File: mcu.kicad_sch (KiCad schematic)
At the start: 18 parts

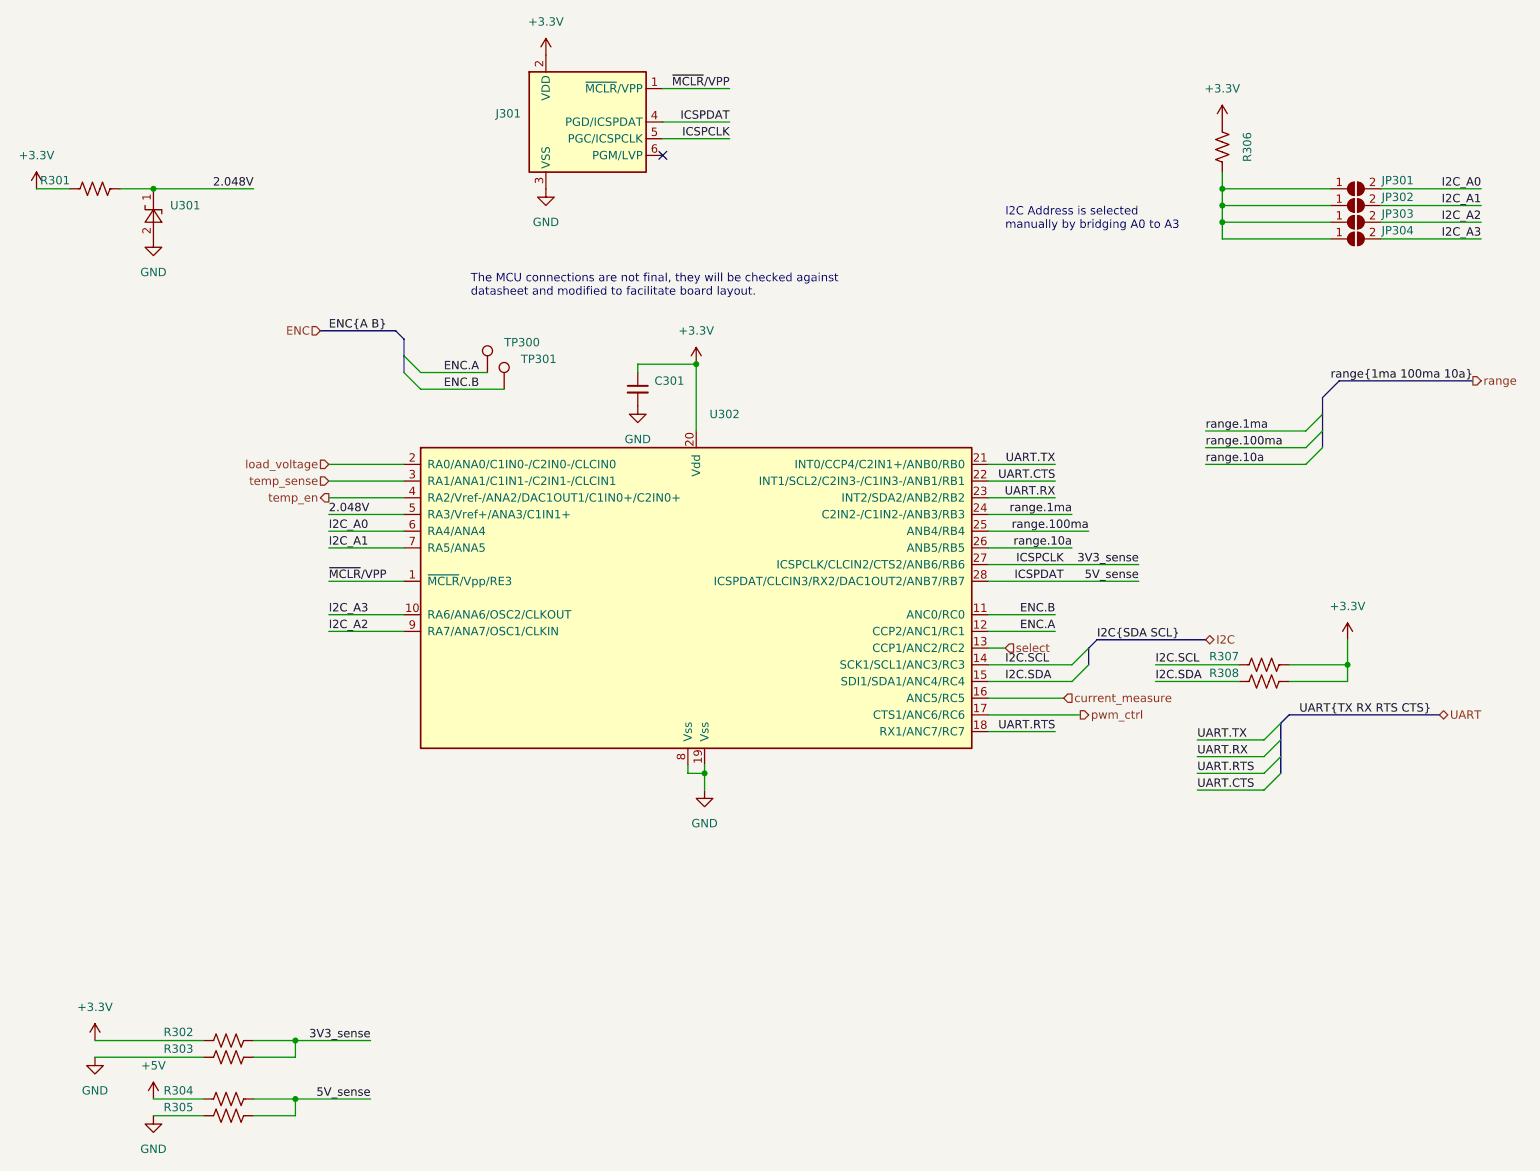
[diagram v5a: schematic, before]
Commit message: Reduce trace resistance of 10mOhm channel
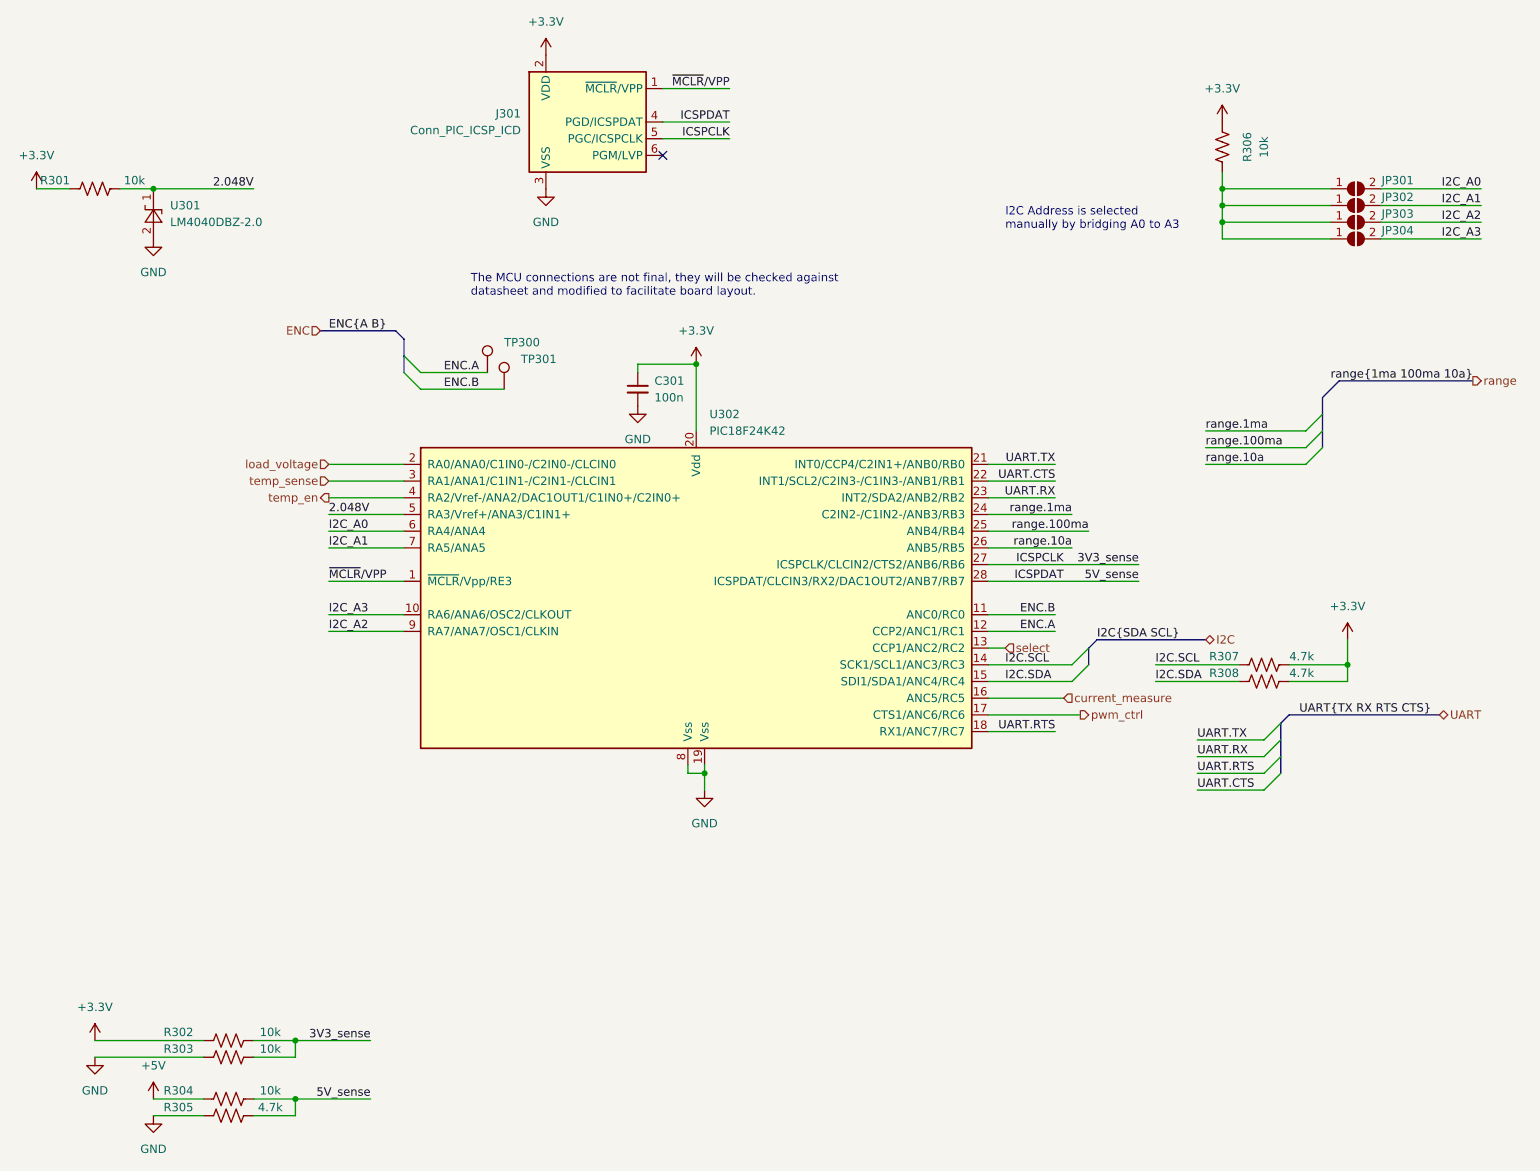
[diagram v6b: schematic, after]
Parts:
- C301: value (none) -> 100n; footprint (none) -> Capacitor_SMD:C_0402_1005Metric
- J301: value (none) -> Conn_PIC_ICSP_ICD; footprint (none) -> Connector_PinHeader_2.54mm:PinHeader_1x06_P2.54mm_Vertical
- JP301, JP302, JP303, JP304: value (none) -> SB; footprint (none) -> Jumper:SolderJumper-2_P1.3mm_Open_TrianglePad1.0x1.5mm
- R301, R302, R303, R304, R306: value (none) -> 10k; footprint (none) -> Resistor_SMD:R_0805_2012Metric
- R305, R307, R308: value (none) -> 4.7k; footprint (none) -> Resistor_SMD:R_0805_2012Metric
- TP300, TP301: value (none) -> ~; footprint (none) -> TestPoint:TestPoint_Pad_D1.0mm
- U301: value (none) -> LM4040DBZ-2.0; footprint (none) -> Package_TO_SOT_SMD:SOT-23
- U302: value (none) -> PIC18F24K42; footprint (none) -> Package_SO:SSOP-28_5.3x10.2mm_P0.65mm
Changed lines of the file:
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@@
       (effects (font (size 1.27 1.27)) (justify right))
     )
-    (property "Value" "" (id 1) (at 236.22 114.3 90)
-      (effects (font (size 1.27 1.27)) (justify right))
-    )
-    (property "Footprint" "" (id 2) (at 228.346 116.586 90)
+    (property "Value" "4.7k" (id 1) (at 236.22 114.3 90)
+      (effects (font (size 1.27 1.27)) (justify right))
+    )
+    (property "Footprint" "Resistor_SMD:R_0805_2012Metric" (id 2) (at 228.346 116.586 90)
       (effects (font (size 1.27 1.27)) hide)
     )
@@
       (effects (font (size 1.27 1.27)) (justify right))
     )
-    (property "Value" "" (id 1) (at 58.42 39.37 90)
-      (effects (font (size 1.27 1.27)) (justify right))
-    )
-    (property "Footprint" "" (id 2) (at 50.546 41.656 90)
+    (property "Value" "10k" (id 1) (at 58.42 39.37 90)
+      (effects (font (size 1.27 1.27)) (justify right))
+    )
+    (property "Footprint" "Resistor_SMD:R_0805_2012Metric" (id 2) (at 50.546 41.656 90)
       (effects (font (size 1.27 1.27)) hide)
     )
@@
       (effects (font (size 1.27 1.27)) (justify left))
     )
-    (property "Value" "" (id 1) (at 113.03 66.5479 0)
-      (effects (font (size 1.27 1.27)) (justify left))
-    )
-    (property "Footprint" "" (id 2) (at 115.57 68.58 0)
+    (property "Value" "~" (id 1) (at 113.03 66.5479 0)
+      (effects (font (size 1.27 1.27)) (justify left))
+    )
+    (property "Footprint" "TestPoint:TestPoint_Pad_D1.0mm" (id 2) (at 115.57 68.58 0)
       (effects (font (size 1.27 1.27)) hide)
     )
@@
       (effects (font (size 1.27 1.27)) (justify right))
     )
-    (property "Value" "" (id 1) (at 115.57 31.7499 0)
-      (effects (font (size 1.27 1.27)) (justify right))
-    )
-    (property "Footprint" "" (id 2) (at 125.73 26.67 0)
+    (property "Value" "Conn_PIC_ICSP_ICD" (id 1) (at 115.57 31.7499 0)
+      (effects (font (size 1.27 1.27)) (justify right))
+    )
+    (property "Footprint" "Connector_PinHeader_2.54mm:PinHeader_1x06_P2.54mm_Vertical" (id 2) (at 125.73 26.67 0)
       (effects (font (size 1.27 1.27)) hide)
     )
@@
     (in_bom no) (on_board yes)
     (property "Reference" "R302" (id 0) (at 63.5 168.91 90))
-    (property "Value" "" (id 1) (at 77.47 168.91 90))
-    (property "Footprint" "" (id 2) (at 70.866 171.196 90)
+    (property "Value" "10k" (id 1) (at 77.47 168.91 90))
+    (property "Footprint" "Resistor_SMD:R_0805_2012Metric" (id 2) (at 70.866 171.196 90)
       (effects (font (size 1.27 1.27)) hide)
     )
@@
     (in_bom no) (on_board yes)
     (property "Reference" "JP301" (id 0) (at 248.92 39.37 0))
-    (property "Value" "" (id 1) (at 242.57 36.83 0)
-      (effects (font (size 1.27 1.27)) hide)
-    )
-    (property "Footprint" "" (id 2) (at 242.57 40.64 0)
+    (property "Value" "SB" (id 1) (at 242.57 36.83 0)
+      (effects (font (size 1.27 1.27)) hide)
+    )
+    (property "Footprint" "Jumper:SolderJumper-2_P1.3mm_Open_TrianglePad1.0x1.5mm" (id 2) (at 242.57 40.64 0)
       (effects (font (size 1.27 1.27)) hide)
     )
@@
     (in_bom no) (on_board yes)
     (property "Reference" "R303" (id 0) (at 63.5 171.45 90))
-    (property "Value" "" (id 1) (at 77.47 171.45 90))
-    (property "Footprint" "" (id 2) (at 71.374 171.704 90)
+    (property "Value" "10k" (id 1) (at 77.47 171.45 90))
+    (property "Footprint" "Resistor_SMD:R_0805_2012Metric" (id 2) (at 71.374 171.704 90)
       (effects (font (size 1.27 1.27)) hide)
     )
@@
       (effects (font (size 1.27 1.27)) (justify left))
     )
-    (property "Value" "" (id 1) (at 115.57 69.0879 0)
-      (effects (font (size 1.27 1.27)) (justify left))
-    )
-    (property "Footprint" "" (id 2) (at 118.11 71.12 0)
+    (property "Value" "~" (id 1) (at 115.57 69.0879 0)
+      (effects (font (size 1.27 1.27)) (justify left))
+    )
+    (property "Footprint" "TestPoint:TestPoint_Pad_D1.0mm" (id 2) (at 118.11 71.12 0)
       (effects (font (size 1.27 1.27)) hide)
     )
@@
       (effects (font (size 1.27 1.27)) (justify left))
     )
-    (property "Value" "" (id 1) (at 144.2594 77.47 0)
-      (effects (font (size 1.27 1.27)) (justify left))
-    )
-    (property "Footprint" "" (id 2) (at 125.73 115.57 0)
+    (property "Value" "PIC18F24K42" (id 1) (at 144.2594 77.47 0)
+      (effects (font (size 1.27 1.27)) (justify left))
+    )
+    (property "Footprint" "Package_SO:SSOP-28_5.3x10.2mm_P0.65mm" (id 2) (at 125.73 115.57 0)
       (effects (font (size 1.27 1.27)) hide)
     )
@@
     (in_bom no) (on_board yes)
     (property "Reference" "R304" (id 0) (at 63.5 177.8 90))
-    (property "Value" "" (id 1) (at 77.47 177.8 90))
-    (property "Footprint" "" (id 2) (at 70.866 180.086 90)
+    (property "Value" "10k" (id 1) (at 77.47 177.8 90))
+    (property "Footprint" "Resistor_SMD:R_0805_2012Metric" (id 2) (at 70.866 180.086 90)
       (effects (font (size 1.27 1.27)) hide)
     )
@@
       (effects (font (size 1.27 1.27)) (justify right))
     )
-    (property "Value" "" (id 1) (at 62.23 45.7199 90)
-      (effects (font (size 1.27 1.27)) (justify right))
-    )
-    (property "Footprint" "" (id 2) (at 64.77 44.45 0)
+    (property "Value" "LM4040DBZ-2.0" (id 1) (at 62.23 45.7199 90)
+      (effects (font (size 1.27 1.27)) (justify right))
+    )
+    (property "Footprint" "Package_TO_SOT_SMD:SOT-23" (id 2) (at 64.77 44.45 0)
       (effects (font (size 1.27 1.27) italic) hide)
     )
@@
       (effects (font (size 1.27 1.27)) (justify left))
     )
-    (property "Value" "" (id 1) (at 135.89 72.3962 0)
-      (effects (font (size 1.27 1.27)) (justify left))
-    )
-    (property "Footprint" "" (id 2) (at 133.35 71.12 0)
+    (property "Value" "100n" (id 1) (at 135.89 72.3962 0)
+      (effects (font (size 1.27 1.27)) (justify left))
+    )
+    (property "Footprint" "Capacitor_SMD:C_0402_1005Metric" (id 2) (at 133.35 71.12 0)
       (effects (font (size 1.27 1.27)) hide)
     )
@@
     (in_bom no) (on_board yes)
     (property "Reference" "R306" (id 0) (at 226.06 34.29 90))
-    (property "Value" "" (id 1) (at 228.6 34.29 90))
-    (property "Footprint" "" (id 2) (at 221.234 34.036 90)
+    (property "Value" "10k" (id 1) (at 228.6 34.29 90))
+    (property "Footprint" "Resistor_SMD:R_0805_2012Metric" (id 2) (at 221.234 34.036 90)
       (effects (font (size 1.27 1.27)) hide)
     )
@@
       (effects (font (size 1.27 1.27)) (justify right))
     )
-    (property "Value" "" (id 1) (at 236.22 111.76 90)
-      (effects (font (size 1.27 1.27)) (justify right))
-    )
-    (property "Footprint" "" (id 2) (at 228.346 114.046 90)
+    (property "Value" "4.7k" (id 1) (at 236.22 111.76 90)
+      (effects (font (size 1.27 1.27)) (justify right))
+    )
+    (property "Footprint" "Resistor_SMD:R_0805_2012Metric" (id 2) (at 228.346 114.046 90)
       (effects (font (size 1.27 1.27)) hide)
     )
@@
     (in_bom no) (on_board yes)
     (property "Reference" "JP303" (id 0) (at 248.92 44.45 0))
-    (property "Value" "" (id 1) (at 242.57 41.91 0)
-      (effects (font (size 1.27 1.27)) hide)
-    )
-    (property "Footprint" "" (id 2) (at 242.57 45.72 0)
+    (property "Value" "SB" (id 1) (at 242.57 41.91 0)
+      (effects (font (size 1.27 1.27)) hide)
+    )
+    (property "Footprint" "Jumper:SolderJumper-2_P1.3mm_Open_TrianglePad1.0x1.5mm" (id 2) (at 242.57 45.72 0)
       (effects (font (size 1.27 1.27)) hide)
     )
@@
     (in_bom no) (on_board yes)
     (property "Reference" "JP304" (id 0) (at 248.92 46.99 0))
-    (property "Value" "" (id 1) (at 242.57 44.45 0)
-      (effects (font (size 1.27 1.27)) hide)
-    )
-    (property "Footprint" "" (id 2) (at 242.57 48.26 0)
+    (property "Value" "SB" (id 1) (at 242.57 44.45 0)
+      (effects (font (size 1.27 1.27)) hide)
+    )
+    (property "Footprint" "Jumper:SolderJumper-2_P1.3mm_Open_TrianglePad1.0x1.5mm" (id 2) (at 242.57 48.26 0)
       (effects (font (size 1.27 1.27)) hide)
     )
@@
     (in_bom no) (on_board yes)
     (property "Reference" "JP302" (id 0) (at 248.92 41.91 0))
-    (property "Value" "" (id 1) (at 242.57 39.37 0)
-      (effects (font (size 1.27 1.27)) hide)
-    )
-    (property "Footprint" "" (id 2) (at 242.57 43.18 0)
+    (property "Value" "SB" (id 1) (at 242.57 39.37 0)
+      (effects (font (size 1.27 1.27)) hide)
+    )
+    (property "Footprint" "Jumper:SolderJumper-2_P1.3mm_Open_TrianglePad1.0x1.5mm" (id 2) (at 242.57 43.18 0)
       (effects (font (size 1.27 1.27)) hide)
     )
@@
     (in_bom no) (on_board yes)
     (property "Reference" "R305" (id 0) (at 63.5 180.34 90))
-    (property "Value" "" (id 1) (at 77.47 180.34 90))
-    (property "Footprint" "" (id 2) (at 71.374 180.594 90)
-      (effects (font (size 1.27 1.27)) hide)
-    )
+    (property "Value" "4.7k" (id 1) (at 77.47 180.34 90))
+    (property "Footprint" "Resistor_SMD:R_0805_2012Metric" (id 2) (at 71.374 180.594 90)
+      (effects (font (size 1.27 1.27)) hide)
+    )

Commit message: Generate interactive bom for main and peripheral variants
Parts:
- R307, R308: variant (none) -> main_only
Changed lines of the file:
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@@
+      (effects (font (size 1.27 1.27)) hide)
+    )
+    (property "variant" "main_only" (id 6) (at 228.6 115.57 0)
       (effects (font (size 1.27 1.27)) hide)
     )
@@
     )
     (property "PartNumber" "Generic" (id 5) (at 50.8 40.64 0)
+      (effects (font (size 1.27 1.27)) hide)
+    )
+    (property "variant" "" (id 6) (at 50.8 40.64 0)
       (effects (font (size 1.27 1.27)) hide)
     )
@@
       (effects (font (size 1.27 1.27)) hide)
     )
+    (property "variant" "" (id 6) (at 110.49 68.58 0)
+      (effects (font (size 1.27 1.27)) hide)
+    )
     (pin "1")
   )
@@
     )
     (property "PartNumber" "Generic" (id 5) (at 124.46 30.48 0)
+      (effects (font (size 1.27 1.27)) hide)
+    )
+    (property "variant" "" (id 6) (at 124.46 30.48 0)
       (effects (font (size 1.27 1.27)) hide)
     )
@@
       (effects (font (size 1.27 1.27)) hide)
     )
+    (property "variant" "" (id 6) (at 71.12 170.18 0)
+      (effects (font (size 1.27 1.27)) hide)
+    )
     (pin "1")
     (pin "2")
@@
       (effects (font (size 1.27 1.27)) hide)
     )
+    (property "variant" "" (id 6) (at 242.57 40.64 0)
+      (effects (font (size 1.27 1.27)) hide)
+    )
     (pin "1")
     (pin "2")
@@
       (effects (font (size 1.27 1.27)) hide)
     )
+    (property "variant" "" (id 6) (at 71.12 172.72 0)
+      (effects (font (size 1.27 1.27)) hide)
+    )
     (pin "1")
     (pin "2")
@@
       (effects (font (size 1.27 1.27)) hide)
     )
+    (property "variant" "" (id 6) (at 113.03 71.12 0)
+      (effects (font (size 1.27 1.27)) hide)
+    )
     (pin "1")
   )
@@
     )
     (property "PartNumber" "PIC18F24K42" (id 5) (at 142.24 102.87 0)
+      (effects (font (size 1.27 1.27)) hide)
+    )
+    (property "variant" "" (id 6) (at 142.24 102.87 0)
       (effects (font (size 1.27 1.27)) hide)
     )
@@
       (effects (font (size 1.27 1.27)) hide)
     )
+    (property "variant" "" (id 6) (at 71.12 179.07 0)
+      (effects (font (size 1.27 1.27)) hide)
+    )
     (pin "1")
     (pin "2")
@@
       (effects (font (size 1.27 1.27)) hide)
     )
+    (property "variant" "" (id 6) (at 59.69 44.45 0)
+      (effects (font (size 1.27 1.27)) hide)
+    )
     (pin "1")
     (pin "2")
@@
       (effects (font (size 1.27 1.27)) hide)
     )
+    (property "variant" "" (id 6) (at 133.35 71.12 0)
+      (effects (font (size 1.27 1.27)) hide)
+    )
     (pin "1")
     (pin "2")
@@
       (effects (font (size 1.27 1.27)) hide)
     )
+    (property "variant" "" (id 6) (at 222.25 34.29 0)
+      (effects (font (size 1.27 1.27)) hide)
+    )
     (pin "1")
     (pin "2")
@@
     )
     (property "PartNumber" "Generic" (id 5) (at 228.6 113.03 0)
+      (effects (font (size 1.27 1.27)) hide)
+    )
+    (property "variant" "main_only" (id 6) (at 228.6 113.03 0)
       (effects (font (size 1.27 1.27)) hide)
     )
@@
       (effects (font (size 1.27 1.27)) hide)
     )
+    (property "variant" "" (id 6) (at 242.57 45.72 0)
+      (effects (font (size 1.27 1.27)) hide)
+    )
     (pin "1")
     (pin "2")
@@
       (effects (font (size 1.27 1.27)) hide)
     )
+    (property "variant" "" (id 6) (at 242.57 48.26 0)
+      (effects (font (size 1.27 1.27)) hide)
+    )
     (pin "1")
     (pin "2")
@@
     )
     (property "PartNumber" "N.A." (id 5) (at 242.57 43.18 0)
+      (effects (font (size 1.27 1.27)) hide)
+    )
+    (property "variant" "" (id 6) (at 242.57 43.18 0)
       (effects (font (size 1.27 1.27)) hide)
     )
@@
       (effects (font (size 1.27 1.27)) hide)
     )
+    (property "variant" "" (id 6) (at 71.12 181.61 0)
+      (effects (font (size 1.27 1.27)) hide)
+    )
